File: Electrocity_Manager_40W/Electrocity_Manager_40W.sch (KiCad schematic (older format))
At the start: 197 parts, among them IC2 MAIN_SHUTDOWN, IC3 RELAY_STATE, IC4 ADC_RST, J1 SERIAL, P1 SWD, P10 EMERGENCY, P11 EMERGENCY, P12 FRAME_GRAND, P13 BATT_IN, P15 OUT_B, P16 BATT_IN, P17 OUT_A, P2 CAN, P3 CAN, P4 EMERGENCY_SIGNAL, P5 EMERGENCY_SIGNAL, P6 12V_OUT, P7 12V_OUT, P9 MAIN_SW, Q1 FET_N, Q2 NPN, Q3 NPN, Q4 FET_N, Q7 FET_N, SW1 RST, SW2 SW0, SW3 SW1, U1 MAX3051, U10 BD9G101G, U11 OUTA_CHECK, U12 LOGO, U13 LOGO, U14 OUTB_CHECK, U15 BD33FA1, U16 LOGO, U17 LOGO, U18 LOGO, U19 MCP2221A, U2 STM32F405RG, U20 OSRB38C9AA, U21 OSRB38C9AA, U22 HSIN_946, U23 LOGO, U25 LOGO, U3 FULL COLOR, U4 AQM0802_BL, U5 AP3211, U6 SI8900, U7 AZ1086H, U8 ACS70331, U9 LOGO, X1 8MHz

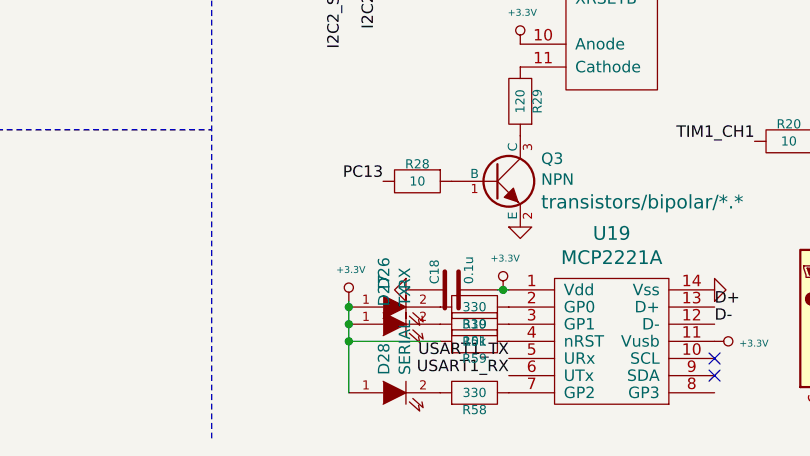
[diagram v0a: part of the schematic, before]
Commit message: MDにモータ駆動用のファンぽーとをつけた
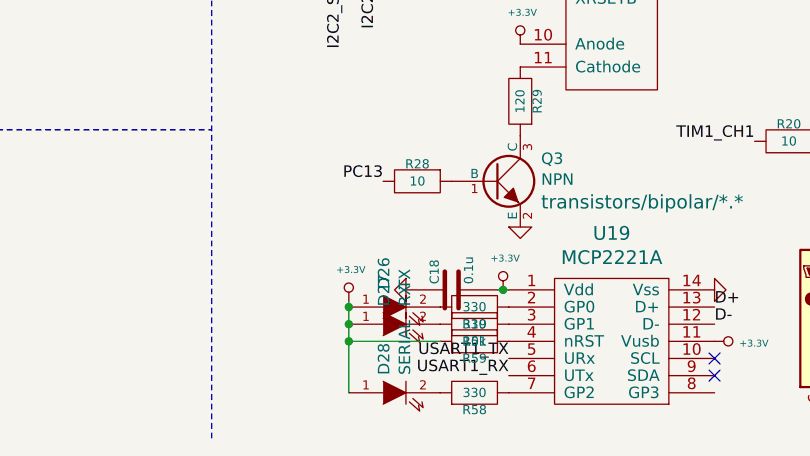
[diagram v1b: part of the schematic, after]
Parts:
- D26: value RX -> TX
- D27: value TX -> RX
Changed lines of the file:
@@
 P 7925 10650
 F 0 "D26" V 7879 10728 50  0000 L CNN
-F 1 "RX" V 7970 10728 50  0000 L CNN
+F 1 "TX" V 7970 10728 50  0000 L CNN
 F 2 "Mizz_lib:LED_0603" H 7925 10650 60  0001 C CNN
 F 3 "" H 7925 10650 60  0000 C CNN
@@
 P 7925 10725
 F 0 "D27" V 7879 10803 50  0000 L CNN
-F 1 "TX" V 7970 10803 50  0000 L CNN
+F 1 "RX" V 7970 10803 50  0000 L CNN
 F 2 "Mizz_lib:LED_0603" H 7925 10725 60  0001 C CNN
 F 3 "" H 7925 10725 60  0000 C CNN

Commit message: normal MD構成大体固まった
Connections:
- net GND: now also DCDC1.1 (-Vout); no longer DCDC1.3 (+Vout)
- net at C35.1, R52.2, U8.1 (IP+)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: now also DCDC1.3 (+Vout); no longer DCDC1.1 (-Vout)
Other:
- moved on the sheet: C35, C41, C42, C44, R43, R47, R52, R53, U8
